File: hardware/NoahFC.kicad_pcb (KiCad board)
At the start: 2 copper layers, 32 x 42 mm, 50 parts, among them J1 ALE, J10 ESC-, J11 CAM, J12 VTX, J2 ELE, J3 VCC, J4 FTDI, J5 GND, J6 THR, J7 PPM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

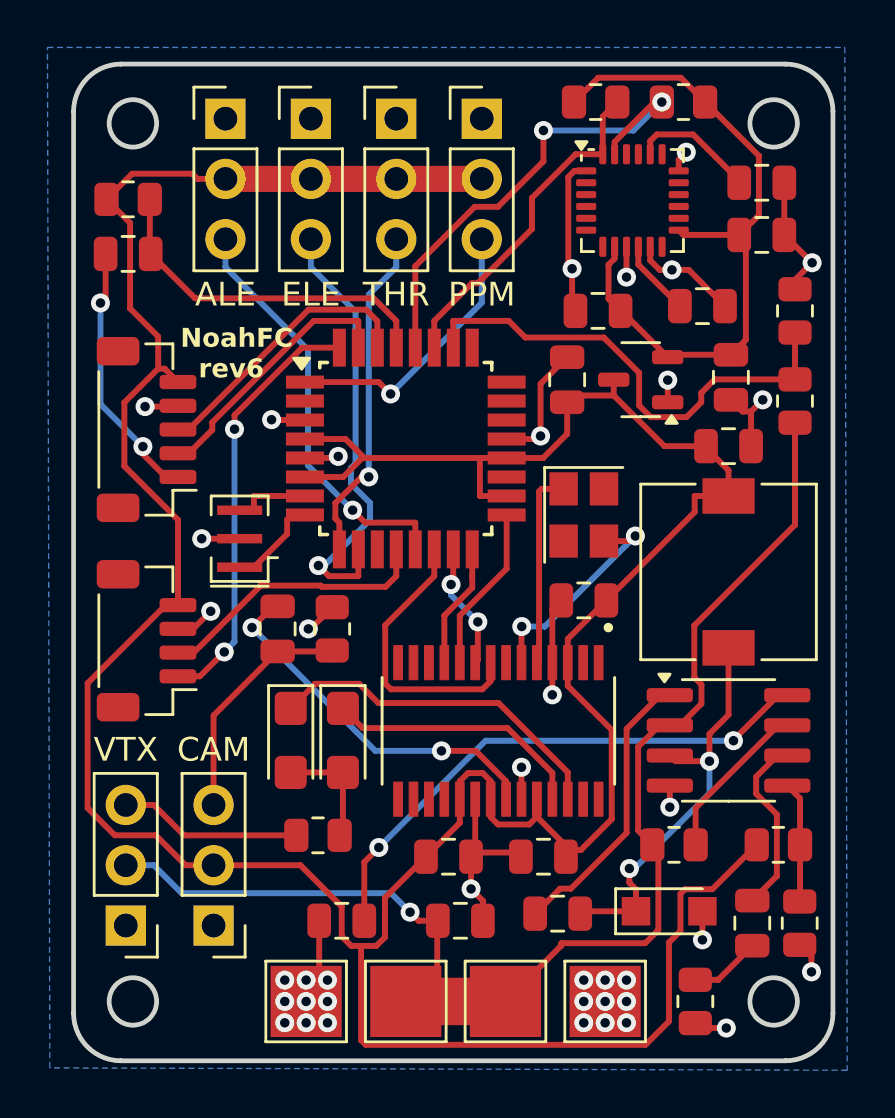
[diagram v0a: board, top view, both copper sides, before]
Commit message: replace buck converter with LM317
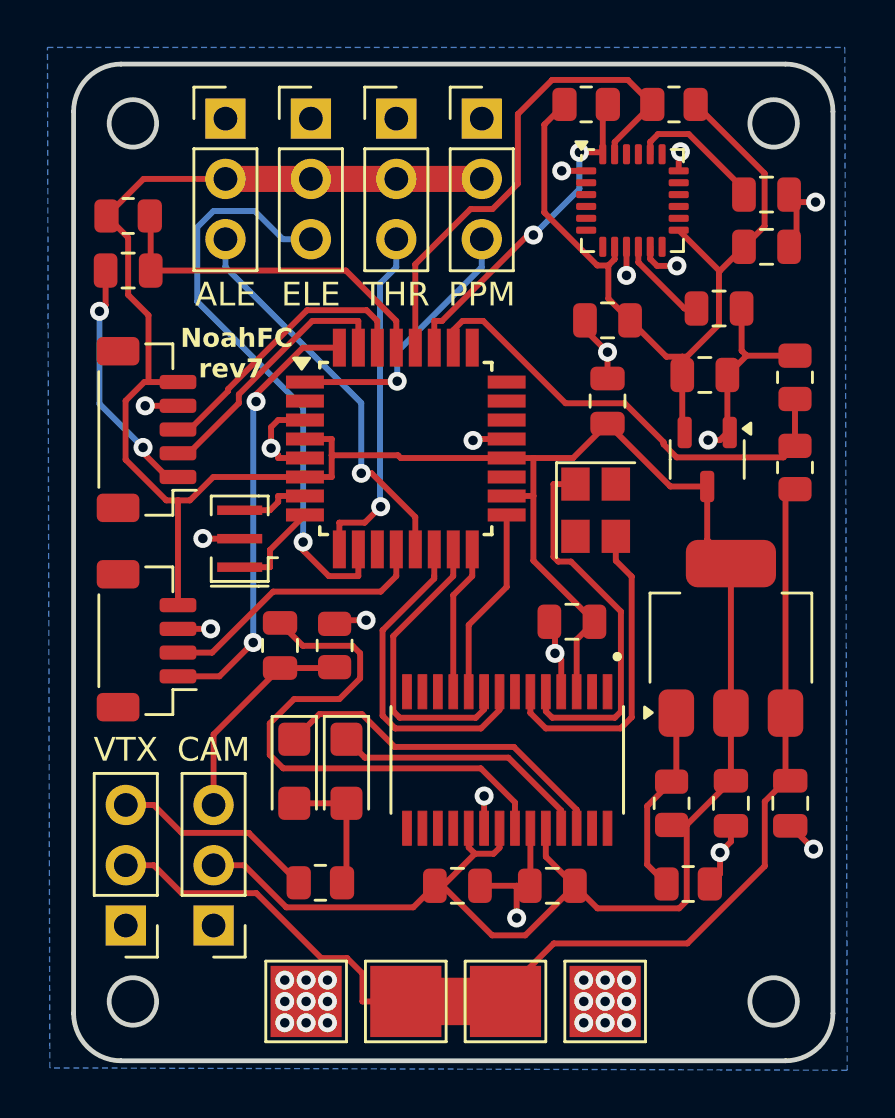
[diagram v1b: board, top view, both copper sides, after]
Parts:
- removed C13, C15: 22uF, Capacitor_SMD:C_0805_2012Metric
- removed C14: 10nF, Capacitor_SMD:C_0805_2012Metric
- removed D4: SS34, Diode_SMD:Nexperia_CFP3_SOD-123W
- removed L1: 10uH, Inductor_SMD:L_7.3x7.3_H3.5
- removed R13: 44.2K, Resistor_SMD:R_0805_2012Metric
- removed R14: 10K, Resistor_SMD:R_0805_2012Metric
- removed R6: 100K, Resistor_SMD:R_0805_2012Metric
- added R2: 240, Resistor_SMD:R_0805_2012Metric, F.Cu at (87.4, 104.3)
- C12: value 3.9nF -> 1uF
- R11: value 6.8K -> 750
- R4: value 10K -> 47K
- R5: value 10K -> 33K
- U4: value MP2303ADN -> LM317_SOT-223; footprint Package_SO:SOIC-8_3.9x4.9mm_P1.27mm -> Package_TO_SOT_SMD:SOT-223-3_TabPin2
- moved C5 19.5 mm to (92.4, 104.3), turned to 90 degrees
- moved C12 5.13 mm to (89.9, 104.3)
- moved R11 4.96 mm to (88.1, 107.8), turned to 180 degrees
- moved U3 4.38 mm to (88.9, 89.9), turned to -90 degrees
- moved U4 4.30 mm to (89.9, 97.4), turned to 90 degrees
- moved R4 2.80 mm to (92.6, 86.4)
- moved R5 2.80 mm to (92.6, 90.2)
- moved R10 2.00 mm to (72.6, 107.7)
- moved C10 1.92 mm to (84.7, 87.4)
- moved C18 1.31 mm to (71.5, 103.0)
- moved C19 1.31 mm to (73.7, 103.0)
- moved C1 1.28 mm to (78.4, 107.8)
- moved C4 1.28 mm to (82.4, 107.8)
- moved U5 1.28 mm to (80.5, 102.5)
- moved C11 1.10 mm to (88.8, 86.3), turned to 180 degrees
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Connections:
- C12 pad 1: Net-(C12-Pad1) -> GND
- C12 pad 2: Net-(U4-COMP) -> 5V
- C5 pad 2: Net-(U4-SS) -> VCC
- R11 pad 2: Net-(C12-Pad1) -> Net-(U4-ADJ)
- U4 pad 1: Net-(U4-BS) -> Net-(U4-ADJ)
- U4 pad 2: VCC -> 5V
- U4 pad 3: Net-(D4-K) -> VCC
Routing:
- net 5V: track 155.5 -> 126.7 mm
- net Net-(U4-SS): track 23.2 -> 0.00 mm, vias 2 -> 0
- net Net-(D4-K): track 17.2 -> 0.00 mm, vias 2 -> 0
- net Net-(U4-BS): track 12.1 -> 0.00 mm
- net GND: track 57.3 -> 45.5 mm, vias 39 -> 36
- net Net-(U4-ADJ): track 0.00 -> 8.05 mm
- net XTAL1_OSD: track 8.33 -> 16.2 mm
- net Net-(U4-COMP): track 7.69 -> 0.00 mm
- net VIN: track 15.6 -> 23.1 mm, vias 2 -> 0
- net MOSI: track 5.33 -> 12.7 mm, vias 2 -> 0
- net Net-(U4-EN): track 6.86 -> 0.00 mm
- net ELEVATOR: track 19.0 -> 24.9 mm
- net VCC: track 54.7 -> 49.4 mm, vias 1 -> 0
- net Net-(U4-FB): track 5.11 -> 0.00 mm
- net XTAL2_OSD: track 9.31 -> 13.5 mm, vias 2 -> 0
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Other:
- board text added: "NoahFC rev7"
- board text removed: "NoahFC rev6"

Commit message: update to rev7 board
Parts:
- removed U5: MAX7456EUI+, MAX7456:SOP65P637X110-28N
- added J13: ESC_GND, TestPoint:TestPoint_Pad_1.0x1.0mm, F.Cu at (64.9, 78.2)
- added J14: ESC_PWM, TestPoint:TestPoint_Pad_1.0x1.0mm, F.Cu at (64.9, 80.3)
- added J15: BEC+, TestPoint:TestPoint_Pad_2.0x2.0mm, F.Cu at (83.1, 78.2)
- added J16: BEC-, TestPoint:TestPoint_Pad_2.0x2.0mm, F.Cu at (83.1, 75.1)
- added U6: MAX7456EUI+, MAX7456:SOP65P637X110-28N, F.Cu at (80.5, 102.6)
- moved R7 10.4 mm to (92.6, 80.5), turned to -90 degrees
- moved R8 10.1 mm to (91.2, 84.3)
- moved C6 9.96 mm to (87.7, 74.5)
- moved R1 8.71 mm to (69.4, 86.8), turned to 90 degrees
- moved C7 8.30 mm to (83.2, 82.2), turned to 90 degrees
- moved C9 7.57 mm to (86.3, 84.3), turned to 180 degrees
- moved C8 7.07 mm to (88.4, 76.5)
- moved U2 3.06 mm to (88.5, 80.3), turned to 180 degrees
- moved Y1 1.81 mm to (69.4, 91.4)
- moved R11 1.73 mm to (89.7, 108.4)
- moved U3 1.14 mm to (88.8, 91.0)
- moved R5 1.12 mm to (92.4, 91.3)
- moved R4 1.02 mm to (92.4, 87.4)
- moved C12 1.00 mm to (89.9, 105.3)
- moved C5 1.00 mm to (92.4, 105.3)
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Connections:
- J1 pad 2: 5V -> BEC_5V
- J2 pad 2: 5V -> BEC_5V
- J6 pad 2: 5V -> BEC_5V
- J7 pad 2: 5V -> BEC_5V
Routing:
- net BEC_5V: track 0.00 -> 26.6 mm, vias 0 -> 1
- net 3.3V: track 34.0 -> 53.7 mm, vias 0 -> 2
- net GND: track 45.5 -> 63.5 mm, vias 36 -> 46
- net THROTTLE: track 14.7 -> 32.2 mm, vias 1 -> 2
- net 5V: track 126.7 -> 115.6 mm, vias 0 -> 4
- net ELEVATOR: track 24.9 -> 15.7 mm
- net TX: track 11.3 -> 19.3 mm, vias 0 -> 2
- net PPM: track 11.4 -> 18.1 mm
- net SDA: track 14.3 -> 20.9 mm
- net Net-(C18-Pad2): track 5.63 -> 9.61 mm, vias 0 -> 2
- net Net-(U2-CPOUT): track 5.79 -> 2.26 mm
- net RESET: track 14.7 -> 17.3 mm
- net Net-(U2-REGOUT): track 3.91 -> 2.18 mm
- net VOLTAGE: track 19.9 -> 21.6 mm, vias 0 -> 2
- net SCL: track 21.6 -> 20.0 mm
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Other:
- board text added: "BEC-5V"
- board text added: "GND"
- board text added: "PWM"
